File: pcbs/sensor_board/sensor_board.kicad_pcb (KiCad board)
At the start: 2 copper layers, 32 x 51 mm, 50 parts, among them J1 1.5mm, J2 2.5mm, J3 2.5mm, J4 1.5 mm, J5 RJ45, J6 Conn_01x06, J7 Conn_01x02, J8 Conn_01x02, Q1 220mA / 50V, Q2 220mA / 50V, Q3 220mA / 50V, U1 8-28V in / 5V 5W out, U2 8x GPIO, U3 4x PWM, U4 1 MOhm, U5 100 kOhm

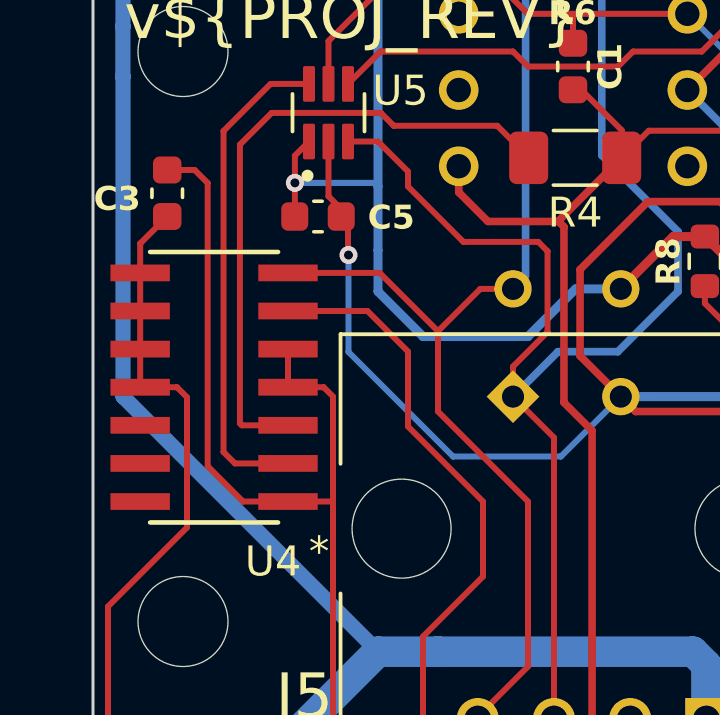
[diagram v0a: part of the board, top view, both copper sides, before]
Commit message: fix sensor board 1 MOhm trimpot wiring error (bumped to version 2.1)
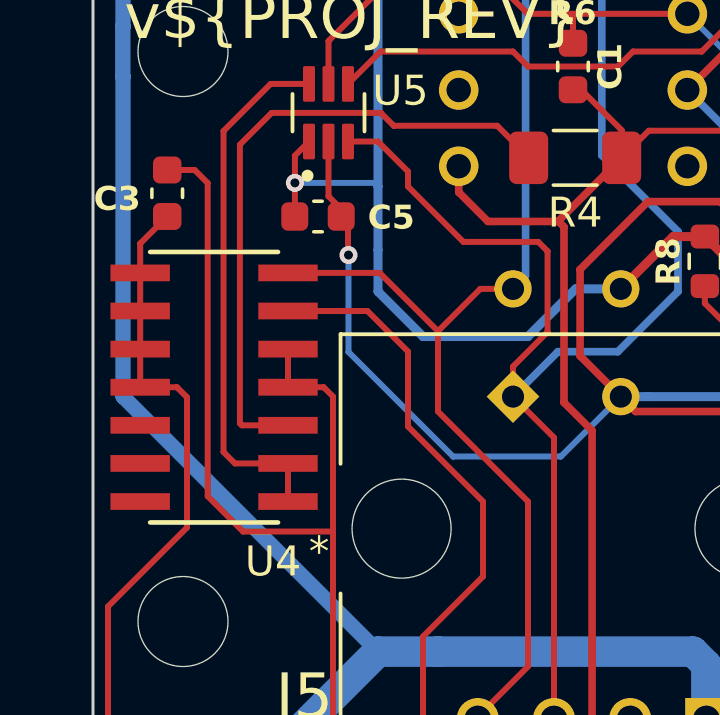
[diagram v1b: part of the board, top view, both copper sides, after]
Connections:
- U4 pad 1: +5V -> Net-(U4-A1)
- U4 pad 2: Net-(U4-W1) -> Net-(U4-A1)
- U5 pad 6: Net-(U4-W1) -> Net-(U4-A1)
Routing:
- net Net-(U4-A1): track 0.00 -> 17.8 mm
- net Net-(U4-W1): track 16.5 -> 0.00 mm
- net +5V: track 196.4 -> 197.4 mm
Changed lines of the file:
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@@
 	)
 	(property "PROJ_AUTHOR" "Sebastian Kopf")
-	(property "PROJ_REV" "2.0")
+	(property "PROJ_REV" "2.1")
 	(property "PROJ_TITLE" "µLogger Sensor Board")
 	(footprint "footprints:SOT-403-1_TSSOP16"
@@
 			(layers "F.Cu" "F.Mask" "F.Paste")
 			(roundrect_rratio 0.125)
-			(net "Net-(U4-W1)")
+			(net "Net-(U4-A1)")
 			(pinfunction "W_6")
 			(pintype "bidirectional")
@@
 			)
 		)
-		(property "Datasheet" "https://www.analog.com/media/en/technical-documentation/data-sheets/AD5241_5242.pdf"
+		(property "Datasheet" "https://www.analog.com/media/en/technical-documentation/data-sheets/ad5241_ad5242.pdf"
 			(at 0 0 0)
 			(layer "F.Fab")
@@
 			(size 1.9812 0.5588)
 			(layers "F.Cu" "F.Mask" "F.Paste")
-			(net "+5V")
+			(net "Net-(U4-A1)")
 			(pinfunction "A1_1")
 			(pintype "unspecified")
@@
 			(size 1.9812 0.5588)
 			(layers "F.Cu" "F.Mask" "F.Paste")
-			(net "Net-(U4-W1)")
+			(net "Net-(U4-A1)")
 			(pinfunction "W1_2")
 			(pintype "unspecified")
@@
 	)
 	(segment
-		(start 140.5 109.5)
-		(end 139 109.5)
-		(width 0.2)
-		(layer "F.Cu")
-		(net "+5V")
-	)
-	(segment
 		(start 140.5 117.825)
 		(end 140.5 109.5)
@@
 	)
 	(segment
-		(start 136.322548 98.882508)
-		(end 135.888536 98.448496)
-		(width 0.2)
-		(layer "F.Cu")
-		(net "+5V")
-	)
-	(segment
-		(start 137.5 109.5)
-		(end 136.322548 108.322548)
-		(width 0.2)
-		(layer "F.Cu")
-		(net "+5V")
-	)
-	(segment
 		(start 147.675 89.5)
 		(end 144.38 86.205)
@@
 	)
 	(segment
-		(start 139 109.5)
-		(end 137.5 109.5)
-		(width 0.2)
+		(start 152.895444 100.668286)
+		(end 154.484873 102.257715)
+		(width 0.3)
 		(layer "F.Cu")
 		(net "+5V")
 	)
 	(segment
-		(start 152.895444 100.668286)
-		(end 154.484873 102.257715)
-		(width 0.3)
+		(start 137.5 110.5)
+		(end 136.322548 109.322548)
+		(width 0.2)
 		(layer "F.Cu")
 		(net "+5V")
@@
 	)
 	(segment
-		(start 154.672195 102.257715)
-		(end 155.703966 103.289486)
-		(width 0.3)
+		(start 136.322548 98.882508)
+		(end 135.888536 98.448496)
+		(width 0.2)
 		(layer "F.Cu")
 		(net "+5V")
 	)
 	(segment
-		(start 147.5 80.915042)
-		(end 145.584958 80.915042)
+		(start 136.322548 109.322548)
+		(end 136.322548 98.882508)
 		(width 0.2)
 		(layer "F.Cu")
@@
 	)
 	(segment
-		(start 151.836414 100.668286)
-		(end 152.895444 100.668286)
+		(start 140.5 110.5)
+		(end 137.5 110.5)
+		(width 0.2)
+		(layer "F.Cu")
+		(net "+5V")
+	)
+	(segment
+		(start 154.672195 102.257715)
+		(end 155.703966 103.289486)
 		(width 0.3)
 		(layer "F.Cu")
@@
 	)
 	(segment
-		(start 135.888536 98.448496)
-		(end 134.974356 98.448496)
+		(start 147.5 80.915042)
+		(end 145.584958 80.915042)
 		(width 0.2)
 		(layer "F.Cu")
@@
 	)
 	(segment
-		(start 145 84.88)
-		(end 144.38 85.5)
-		(width 0.2)
+		(start 151.836414 100.668286)
+		(end 152.895444 100.668286)
+		(width 0.3)
 		(layer "F.Cu")
 		(net "+5V")
 	)
 	(segment
-		(start 136.322548 108.322548)
-		(end 136.322548 98.882508)
+		(start 145 84.88)
+		(end 144.38 85.5)
 		(width 0.2)
 		(layer "F.Cu")
@@
 	)
 	(segment
+		(start 135.888536 98.448496)
+		(end 134.974356 98.448496)
+		(width 0.2)
+		(layer "F.Cu")
+		(net "+5V")
+	)
+	(segment
 		(start 139.325 119)
 		(end 140.5 117.825)
@@
 	)
 	(segment
-		(start 137.23 108.23)
-		(end 136.851041 107.851041)
-		(width 0.2)
-		(layer "F.Cu")
-		(net "Net-(U4-W1)")
-	)
-	(segment
-		(start 136.851041 107.851041)
-		(end 136.851041 97.148959)
-		(width 0.2)
-		(layer "F.Cu")
-		(net "Net-(U4-W1)")
-	)
-	(segment
-		(start 136.851041 97.148959)
-		(end 138.42 95.58)
-		(width 0.2)
-		(layer "F.Cu")
-		(net "Net-(U4-W1)")
-	)
-	(segment
-		(start 139 108.23)
-		(end 137.23 108.23)
-		(width 0.2)
-		(layer "F.Cu")
-		(net "Net-(U4-W1)")
-	)
-	(segment
-		(start 138.42 95.58)
-		(end 139.7 95.58)
-		(width 0.2)
-		(layer "F.Cu")
-		(net "Net-(U4-W1)")
-	)
-	(segment
 		(start 137.2 117.7)
 		(end 137.675 118.175)
@@
 		(net "Net-(JP2-B)")
 	)
+	(segment
+		(start 139 109.5)
+		(end 139 108.23)
+		(width 0.2)
+		(layer "F.Cu")
+		(net "Net-(U4-A1)")
+	)
+	(segment
+		(start 137.23 108.23)
+		(end 136.851041 107.851041)
+		(width 0.2)
+		(layer "F.Cu")
+		(net "Net-(U4-A1)")
+	)
+	(segment
+		(start 136.851041 107.851041)
+		(end 136.851041 97.148959)
+		(width 0.2)
+		(layer "F.Cu")
+		(net "Net-(U4-A1)")
+	)
+	(segment
+		(start 136.851041 97.148959)
+		(end 138.42 95.58)
+		(width 0.2)
+		(layer "F.Cu")
+		(net "Net-(U4-A1)")
+	)
+	(segment
+		(start 139 108.23)
+		(end 137.23 108.23)
+		(width 0.2)
+		(layer "F.Cu")
+		(net "Net-(U4-A1)")
+	)
+	(segment
+		(start 138.42 95.58)
+		(end 139.7 95.58)
+		(width 0.2)
+		(layer "F.Cu")
+		(net "Net-(U4-A1)")
+	)
 	(embedded_fonts no)
